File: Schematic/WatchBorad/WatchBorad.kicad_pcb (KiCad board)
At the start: 4 copper layers, 35 x 35 mm, 116 parts, among them J3 TYPE-C-31-M-17, M1 Motor_DC, SW1 SW_Push, SW2 SW_Push, SW3 SW_Push, SW4 SW_Push, SW5 SW_Push, U1 LSM6DSRTR, U10 M41T62Q6F, U11 GC9A01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

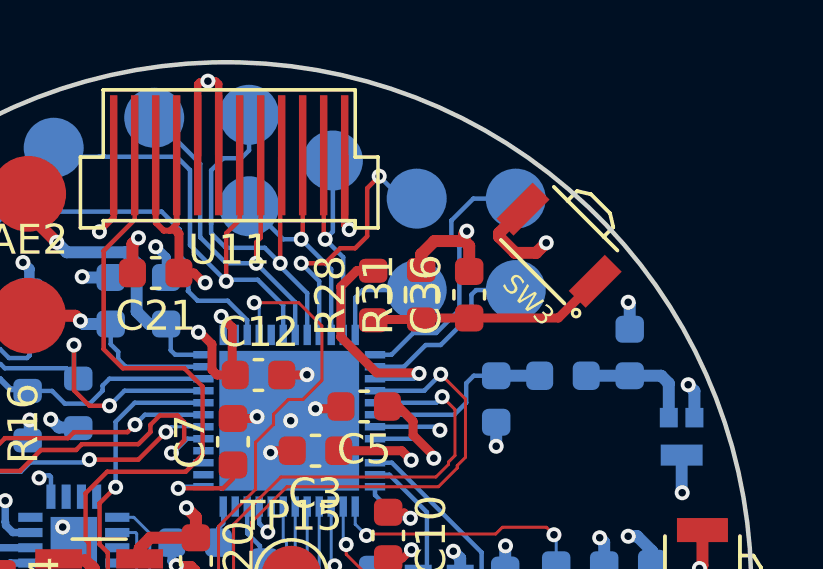
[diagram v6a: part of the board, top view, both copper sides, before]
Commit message: Fixed PCB layout for GND pads near the buttons [PCB]
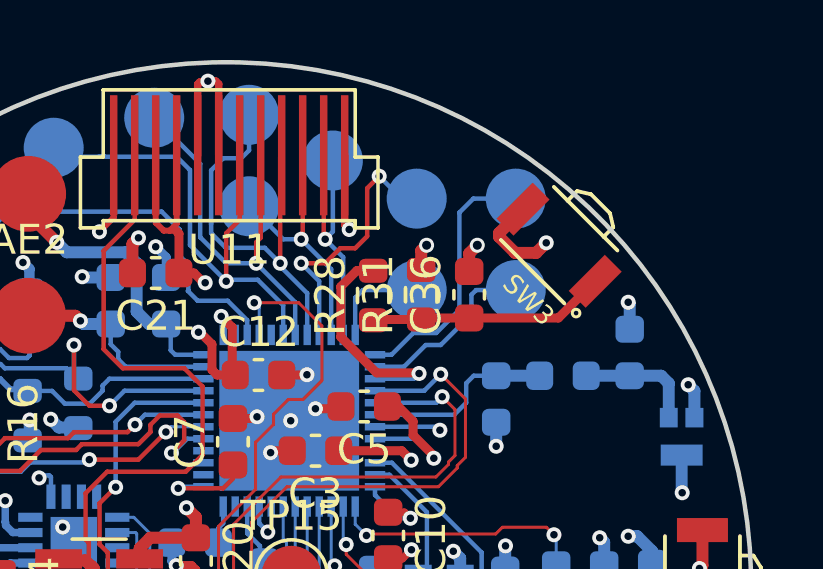
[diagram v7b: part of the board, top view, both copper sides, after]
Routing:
- net GND: track 105.8 -> 104.1 mm, vias 75 -> 76

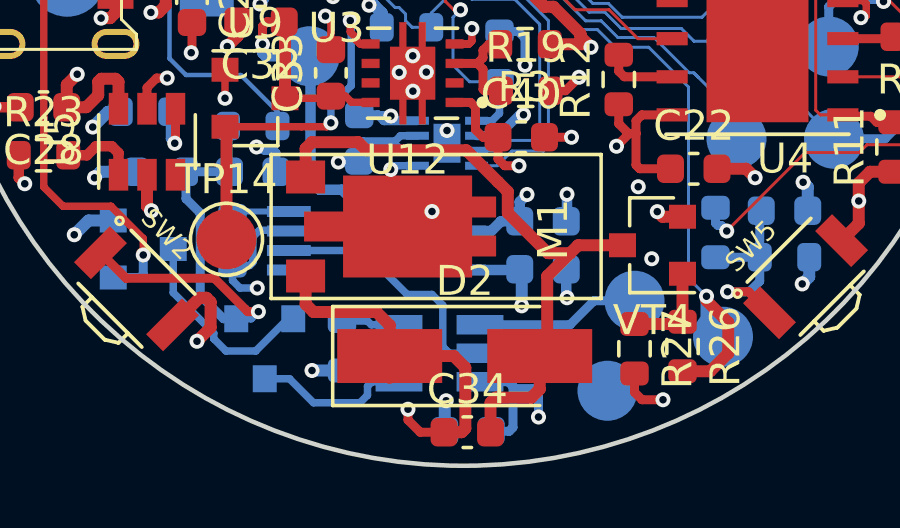
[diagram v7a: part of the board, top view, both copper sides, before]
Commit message: Added D-trigger instead of the MAX switching chip
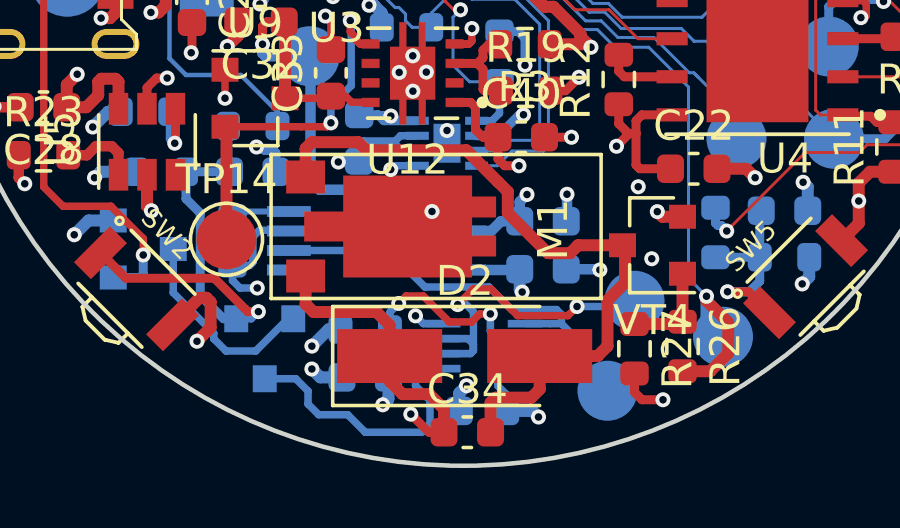
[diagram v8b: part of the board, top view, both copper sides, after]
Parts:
- added C8: 100 nF, Capacitor_SMD:C_0603_1608Metric, B.Cu at (85.6, 103.5)
- U7: value max16054azt+t -> SN74LVC2G74-EP_DCU_8; footprint TO_SOT_Packages_SMD:SOT-23-6_Handsoldering -> SN74LVC2G74:SN74LVC2G74
- moved U7 1.50 mm to (89.6, 102.4)
- moved R21 0.95 mm to (85.6, 101.9), turned to 0 degrees
- moved C29 0.83 mm to (89.5, 104.6)
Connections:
- R21 pad 1: Net-(R21-Pad1) -> +BATT
- R21 pad 2: GND -> Net-(R21-Pad2)
- U7 pad 2: GND -> Net-(TP20-Pad1)
- U7 pad 3: Net-(R21-Pad1) -> Net-(TP20-Pad1)
- U7 pad 4: Net-(TP20-Pad1) -> GND
- U7 pad 6: +BATT -> Net-(R21-Pad2)
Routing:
- net Net-(R21-Pad2): track 0.00 -> 6.45 mm, vias 0 -> 2
- net Net-(TP20-Pad1): track 5.48 -> 11.0 mm, vias 0 -> 2
- net Net-(U7-Pad1): track 5.36 -> 9.67 mm
- net Net-(C34-Pad2): track 21.4 -> 24.0 mm
- net +3V3: track 78.4 -> 76.4 mm
- net Net-(R21-Pad1): track 1.95 -> 0.00 mm
- net GND: track 104.1 -> 103.0 mm, vias 76 -> 77
- net /PSU_logic/PWR_SW_EN_N: track 13.4 -> 14.4 mm
- net +BATT: track 30.1 -> 30.7 mm, vias 10 -> 12
- net +5V: track 24.1 -> 23.6 mm
